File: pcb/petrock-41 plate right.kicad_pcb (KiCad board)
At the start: 2 copper layers, 119.3 x 87.9 mm, 20 parts, among them SW1 SW_PUSH, SW10 SW_PUSH, SW11 SW_PUSH, SW12 SW_PUSH, SW13 SW_PUSH, SW14 SW_PUSH, SW15 SW_PUSH, SW16 SW_PUSH, SW17 SW_PUSH, SW18 SW_PUSH, SW19 SW_PUSH, SW2 SW_PUSH, SW20 SW_PUSH, SW3 SW_PUSH, SW4 SW_PUSH, SW5 SW_PUSH, SW6 SW_PUSH, SW7 SW_PUSH, SW8 SW_PUSH, SW9 SW_PUSH

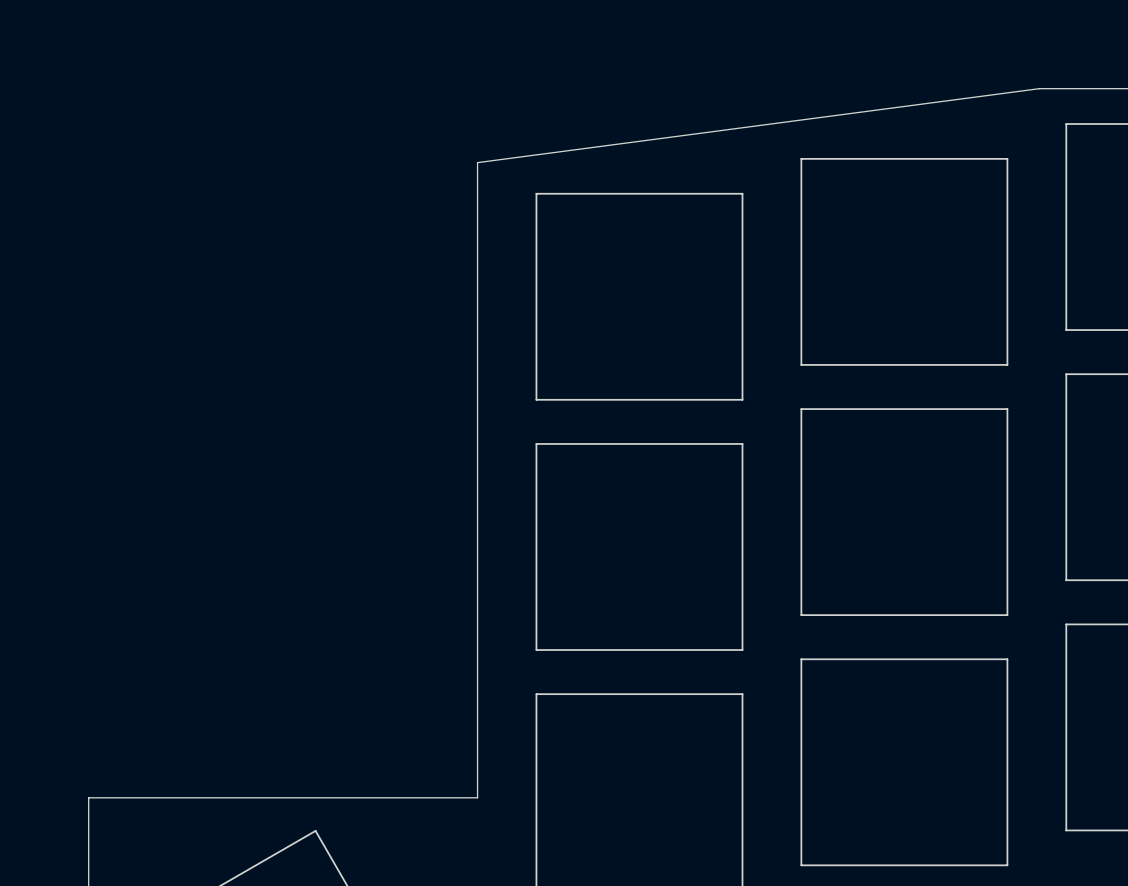
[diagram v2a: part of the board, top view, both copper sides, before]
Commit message: Five standoffs per half, logo on the board, plain controller corner
The standoff the outer pinky column lost moves to where the pinky and ring
columns meet, so the outer top corner is supported again (10 in all). The
logo is back on the board's silkscreen. The jack, reset button and OLED
header lose their printed outlines. The plate's opening by the controller
now starts at the inner index keycap line instead of the stock plate's
fixed edge, clearing the moved controller's sockets by 1.66 mm. The board
records its ENIG finish; renders can hide the jack and reset ("wireless").
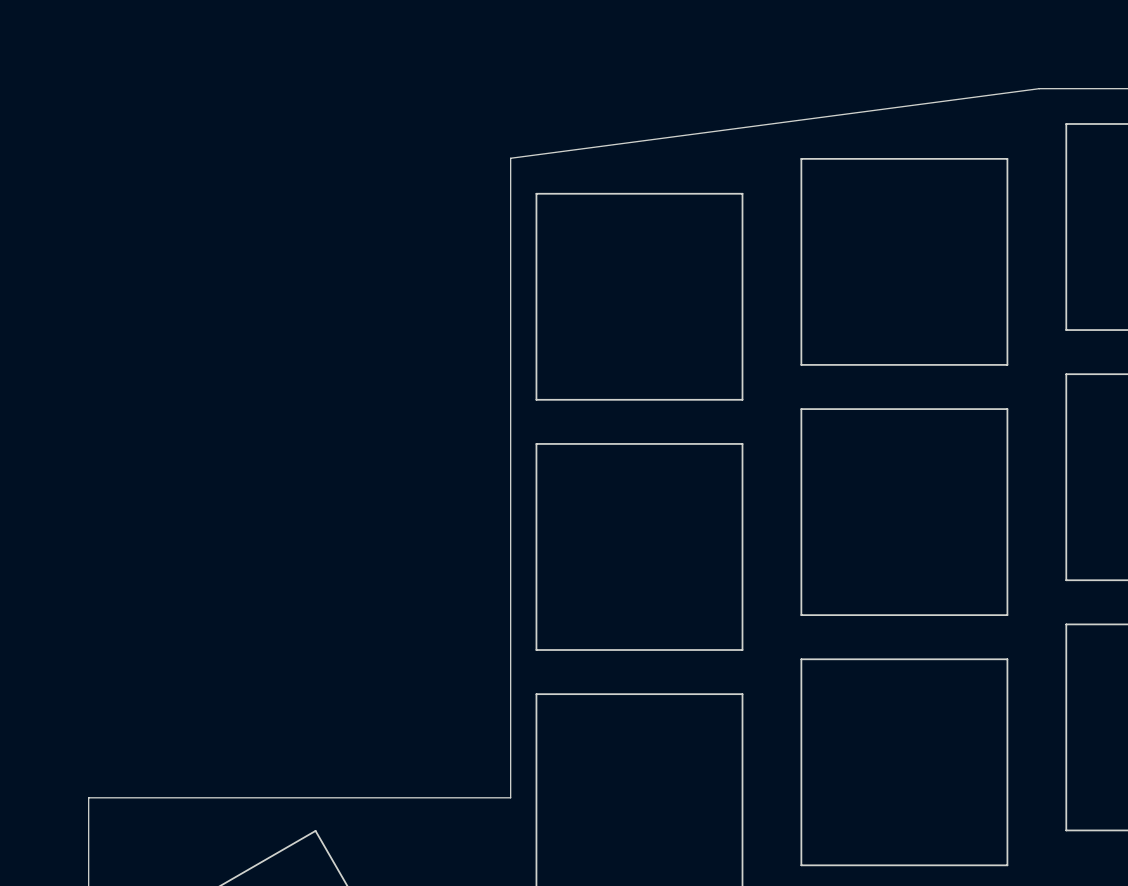
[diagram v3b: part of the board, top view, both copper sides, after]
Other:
- outline, holes or cut-outs redrawn
